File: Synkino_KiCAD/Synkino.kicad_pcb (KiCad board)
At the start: 2 copper layers, 93.3 x 82.3 mm, 181 parts, among them J1 Pwr, J10 EYE8_OUT, J11 EYE4_OUT, J12 2.5mm, J13 EYE5_OUT, J2 2.5mm, J3 3.5mm, J4 Micro_SD_Card_Det_Hirose_DM3AT, J5 EYE1_OUT, J6 EYE6_OUT, J7 EYE2_OUT, J8 EYE7_OUT, J9 EYE3_OUT, Q1 IRF7319, Q2 BC847, Q3 IRLML2244, SW1 SW_Push, SW2 Rotary_Encoder_Switch, SW3 SW_Push, U1 MCP1702T-5002E/MB, U10 ATMEGA328P-AU, U11 QRE1113, U12 QRE1113, U13 QRE1113, U14 QRE1113, U15 QRE1113, U16 QRE1113, U18 QRE1113, U2 ATMEGA328P-AU, U3 74HC4050, U4 SPIOLED128x64, U5 AP7312-1833W6-7, U6 74HC14, U7 VS1053B, U8 MAX4741, U9 QRE1113, X1 FTDIconn, X2 ICSP, X3 FTDIconn, X4 ICSP, Y1 16Mhz, Y2 12.288MHz, Y3 16Mhz

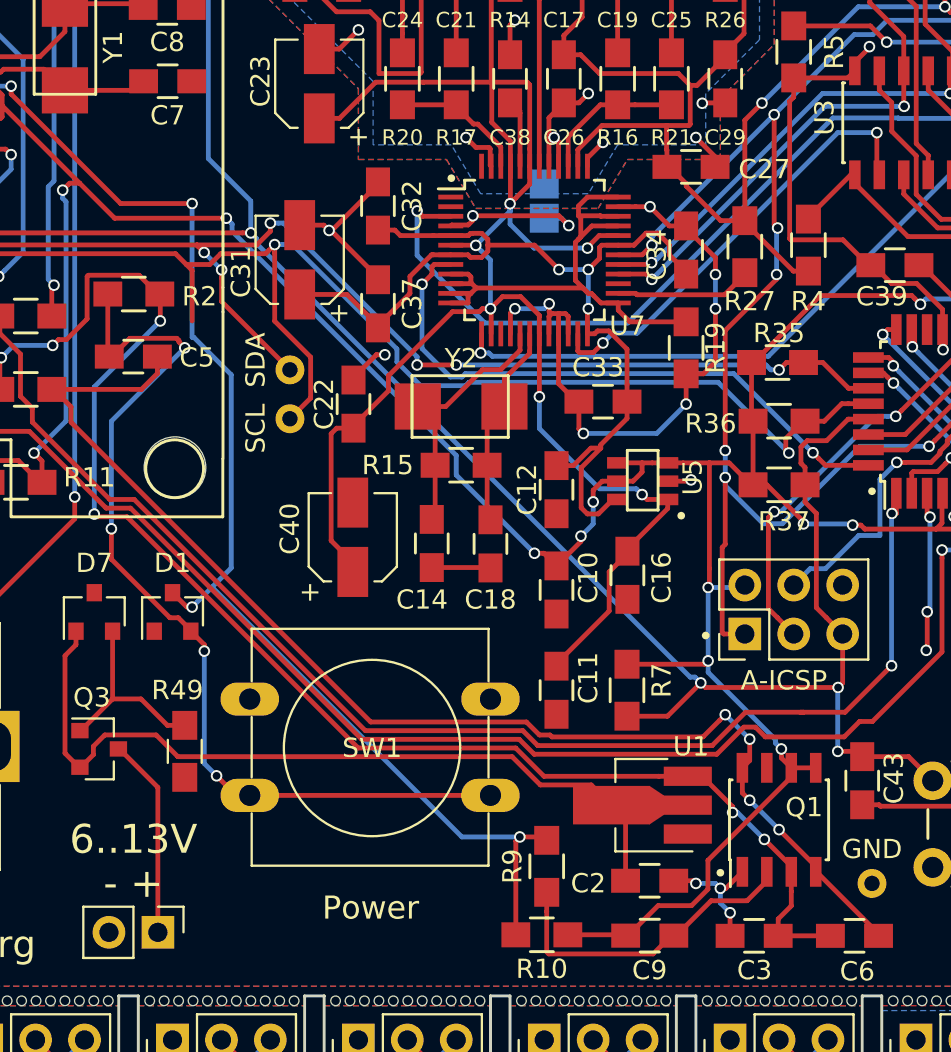
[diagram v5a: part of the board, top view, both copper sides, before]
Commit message: wider 1v8 lines
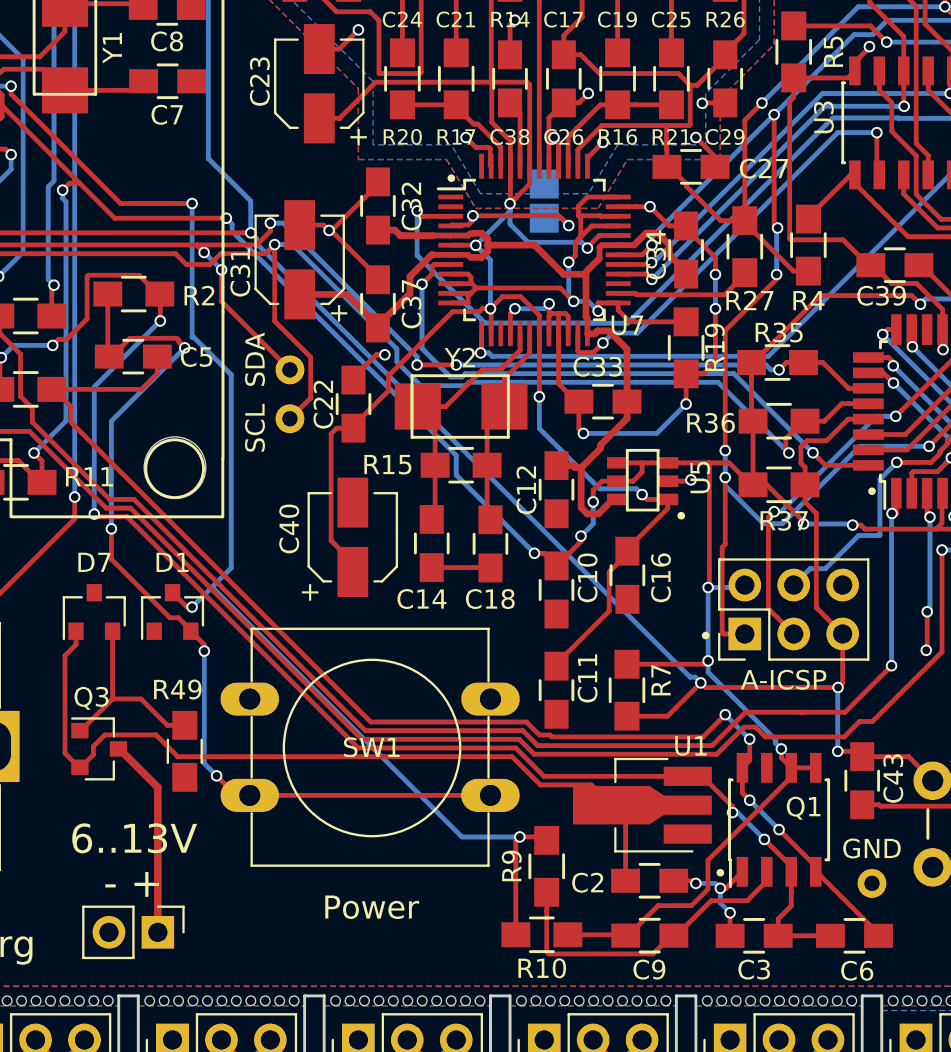
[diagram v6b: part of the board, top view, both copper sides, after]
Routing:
- net /SCL: track 74.7 -> 71.6 mm
- net +1V8: track 52.7 -> 51.6 mm, vias 3 -> 0
- net /GPIO_PLLDWN: track 29.8 -> 30.8 mm, vias 0 -> 3

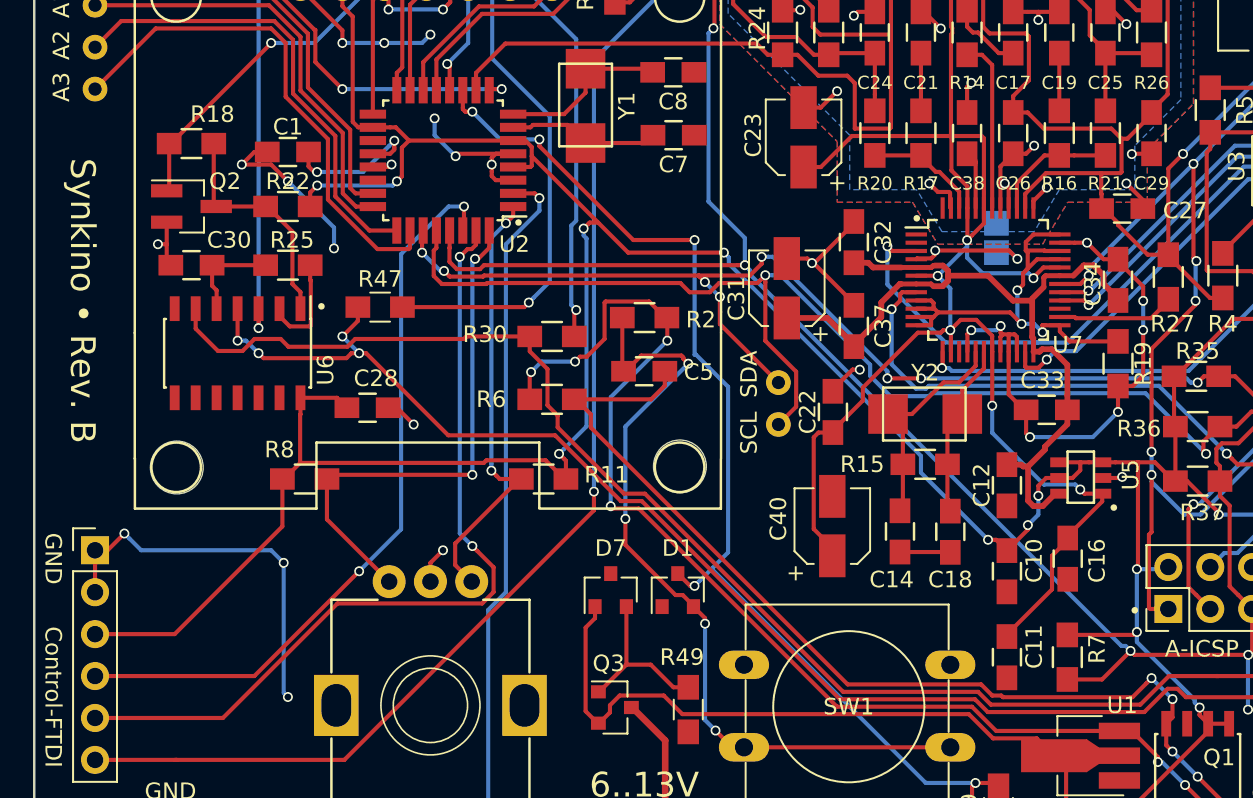
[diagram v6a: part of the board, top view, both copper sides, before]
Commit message: Fix Display Hole Position
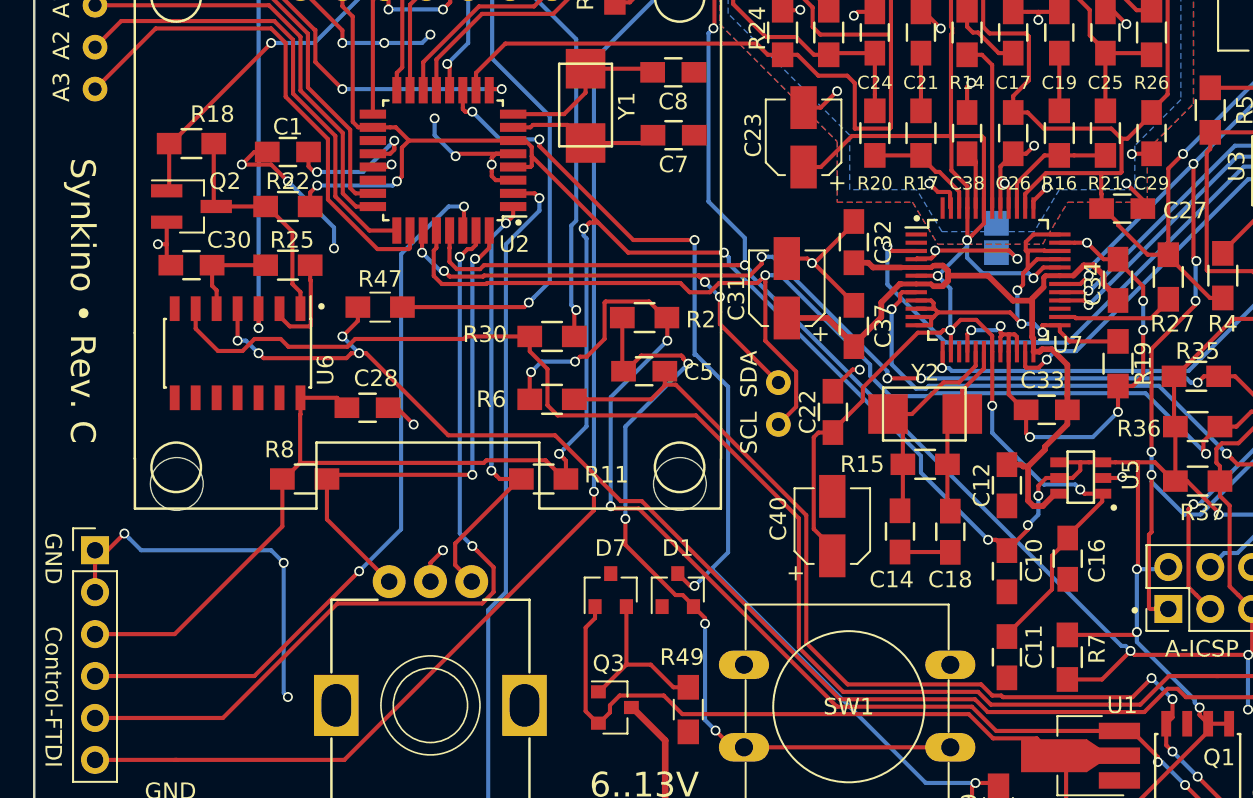
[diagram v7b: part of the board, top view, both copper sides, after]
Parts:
- moved   1.00 mm to (75.3, 81.1)
- moved   1.00 mm to (105.8, 81.0)
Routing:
- net /FlickImp: track 91.6 -> 95.8 mm
- net Net-(C5-Pad1): track 65.2 -> 64.2 mm
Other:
- board text added: "Synkino • Rev. C"
- board text removed: "Synkino • Rev. B"
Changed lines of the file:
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@@
     (links 375)
     (no_connects 0)
-    (area 66.599999 38.024999 160.095001 120.471001)
+    (area 57.856429 32.843999 168.838572 132.270286)
     (thickness 1.6)
     (drawings 107)
-    (tracks 2118)
+    (tracks 2119)
     (zones 0)
     (modules 181)
@@
     (mod_text_size 1 1)
     (mod_text_width 0.15)
-    (pad_size 3.048 1.7272)
-    (pad_drill 1.1)
+    (pad_size 3.2 3.2)
+    (pad_drill 3.2)
     (pad_to_mask_clearance 0.2)
     (aux_axis_origin 71.12 121.92)
@@
   )
   (module Mounting_Holes:MountingHole_3.2mm_M3_DIN965 (layer F.Cu)
-    (at 75.311 80.0735)
+    (at 75.311 81.0735)
     (descr "Mounting Hole 3.2mm, no annular, M3, DIN965")
     (tags "mounting hole 3.2mm no annular m3 din965")
@@
     (fp_circle (center 0 0) (end 2.8 0) (layer Cmts.User) (width 0.15))
     (fp_circle (center 0 0) (end 3.05 0) (layer F.CrtYd) (width 0.05))
-    (pad 1 np_thru_hole circle (at 0 0) (size 3.2 3.2) (drill 3.2) (layers *.Cu *.Mask))
+    (pad "" np_thru_hole circle (at 0 0) (size 3.2 3.2) (drill 3.2) (layers *.Cu *.Mask))
   )
   (module lib_fp:Eye_Mousebites (layer F.Cu)
@@
   )
   (module Mounting_Holes:MountingHole_3.2mm_M3_DIN965 (layer F.Cu)
-    (at 105.791 80.01)
+    (at 105.791 81.01)
     (descr "Mounting Hole 3.2mm, no annular, M3, DIN965")
     (tags "mounting hole 3.2mm no annular m3 din965")
@@
     (fp_circle (center 0 0) (end 2.8 0) (layer Cmts.User) (width 0.15))
     (fp_circle (center 0 0) (end 3.05 0) (layer F.CrtYd) (width 0.05))
-    (pad 1 np_thru_hole circle (at 0 0) (size 3.2 3.2) (drill 3.2) (layers *.Cu *.Mask))
+    (pad "" np_thru_hole circle (at 0 0.0635) (size 3.2 3.2) (drill 3.2) (layers *.Cu *.Mask))
   )
   (module Buttons_Switches_THT:SW_PUSH_6mm_h5mm (layer F.Cu)
@@
     (effects (font (size 1 1) (thickness 0.2)))
   )
-  (gr_text "Synkino • Rev. B" (at 69.596 69.85 270) (layer B.SilkS)
+  (gr_text "Synkino • Rev. C" (at 69.596 69.85 270) (layer B.SilkS)
     (effects (font (size 1.5 1.5) (thickness 0.3)) (justify mirror))
   )
@@
     (effects (font (size 1.4 1.4) (thickness 0.25)) (justify mirror))
   )
-  (gr_text "Synkino • Rev. B" (at 69.596 69.977 270) (layer F.SilkS)
+  (gr_text "Synkino • Rev. C" (at 69.596 69.977 270) (layer F.SilkS)
     (effects (font (size 1.5 1.5) (thickness 0.3)))
   )
@@
   (segment (start 85.461002 97.79) (end 100.584 82.667002) (width 0.25) (layer F.Cu) (net 5))
   (via (at 100.584 81.534) (size 0.6) (drill 0.4) (layers F.Cu B.Cu) (net 5))
-  (segment (start 133.210999 93.992001) (end 134.066001 93.136999) (width 0.25) (layer F.Cu) (net 6))
-  (segment (start 125.266643 93.892001) (end 125.366643 93.992001) (width 0.25) (layer F.Cu) (net 6))
-  (segment (start 125.366643 93.992001) (end 133.210999 93.992001) (width 0.25) (layer F.Cu) (net 6))
+  (segment (start 105.53841 75.057) (end 104.877 75.057) (width 0.25) (layer F.Cu) (net 6))
+  (segment (start 113.448988 82.967577) (end 105.53841 75.057) (width 0.25) (layer F.Cu) (net 6))
+  (segment (start 115.955597 93.216955) (end 113.448988 90.710346) (width 0.25) (layer F.Cu) (net 6))
+  (segment (start 124.042953 93.216955) (end 115.955597 93.216955) (width 0.25) (layer F.Cu) (net 6))
+  (segment (start 124.717999 93.892001) (end 124.042953 93.216955) (width 0.25) (layer F.Cu) (net 6))
+  (segment (start 125.266643 93.892001) (end 124.717999 93.892001) (width 0.25) (layer F.Cu) (net 6))
+  (segment (start 125.366643 93.992001) (end 125.266643 93.892001) (width 0.25) (layer F.Cu) (net 6))
+  (segment (start 133.210999 93.992001) (end 125.366643 93.992001) (width 0.25) (layer F.Cu) (net 6))
+  (segment (start 134.366 92.837) (end 133.210999 93.992001) (width 0.25) (layer F.Cu) (net 6))
+  (segment (start 113.448988 90.710346) (end 113.448988 82.967577) (width 0.25) (layer F.Cu) (net 6))
+  (segment (start 104.877 75.118) (end 104.877 75.057) (width 0.25) (layer F.Cu) (net 6))
+  (segment (start 104.877 75.057) (end 104.877 74.243) (width 0.25) (layer F.Cu) (net 6))
   (segment (start 99.394 75.946) (end 99.494 75.946) (width 0.25) (layer F.Cu) (net 6))
-  (segment (start 124.042953 93.216955) (end 124.717999 93.892001) (width 0.25) (layer F.Cu) (net 6))
-  (segment (start 134.066001 93.136999) (end 134.366 92.837) (width 0.25) (layer F.Cu) (net 6))
-  (segment (start 100.394 77.655356) (end 115.955597 93.216955) (width 0.25) (layer F.Cu) (net 6))
-  (segment (start 124.717999 93.892001) (end 125.266643 93.892001) (width 0.25) (layer F.Cu) (net 6))
-  (segment (start 100.394 76.846) (end 100.394 77.655356) (width 0.25) (layer F.Cu) (net 6))
-  (segment (start 99.494 75.946) (end 100.394 76.846) (width 0.25) (layer F.Cu) (net 6))
-  (segment (start 115.955597 93.216955) (end 124.042953 93.216955) (width 0.25) (layer F.Cu) (net 6))
   (segment (start 135.636 94.107) (end 135.636 95.217) (width 0.25) (layer F.Cu) (net 6))
   (segment (start 135.636 95.217) (end 135.255 95.598) (width 0.25) (layer F.Cu) (net 6))
@@
   (segment (start 99.394 75.946) (end 104.049 75.946) (width 0.25) (layer F.Cu) (net 6))
   (segment (start 104.049 75.946) (end 104.877 75.118) (width 0.25) (layer F.Cu) (net 6))
-  (segment (start 104.877 75.118) (end 104.877 74.243) (width 0.25) (layer F.Cu) (net 6))
   (segment (start 137.16 98.806) (end 139.065 100.711) (width 0.25) (layer F.Cu) (net 6))
   (segment (start 139.065 100.711) (end 139.065 100.998) (width 0.25) (layer F.Cu) (net 6))
@@
   (segment (start 134.332999 71.032001) (end 129.785001 71.032001) (width 0.25) (layer F.Cu) (net 56))
   (segment (start 129.71 70.957) (end 128.81 70.957) (width 0.25) (layer F.Cu) (net 56))
+  (segment (start 106.766001 76.921001) (end 112.998977 83.153977) (width 0.25) (layer F.Cu) (net 57))
+  (segment (start 112.998977 83.153977) (end 112.998977 90.989151) (width 0.25) (layer F.Cu) (net 57))
+  (segment (start 112.998977 90.989151) (end 115.676792 93.666966) (width 0.25) (layer F.Cu) (net 57))
+  (segment (start 98.383999 76.921001) (end 106.766001 76.921001) (width 0.25) (layer F.Cu) (net 57))
   (segment (start 96.694 73.036) (end 96.694 72.136) (width 0.25) (layer F.Cu) (net 57))
   (segment (start 97.769001 74.111001) (end 96.694 73.036) (width 0.25) (layer F.Cu) (net 57))
   (segment (start 97.769001 76.306003) (end 97.769001 74.111001) (width 0.25) (layer F.Cu) (net 57))
   (segment (start 98.383999 76.921001) (end 97.769001 76.306003) (width 0.25) (layer F.Cu) (net 57))
-  (segment (start 115.676792 93.666966) (end 103.669802 81.659976) (width 0.25) (layer F.Cu) (net 57))
   (segment (start 123.856553 93.666966) (end 115.676792 93.666966) (width 0.25) (layer F.Cu) (net 57))
   (segment (start 133.685992 94.442012) (end 124.631599 94.442012) (width 0.25) (layer F.Cu) (net 57))
@@
   (segment (start 138.43 92.71) (end 135.418004 92.71) (width 0.25) (layer F.Cu) (net 57))
   (segment (start 124.631599 94.442012) (end 123.856553 93.666966) (width 0.25) (layer F.Cu) (net 57))
-  (segment (start 103.669802 81.659976) (end 102.40208 81.659976) (width 0.25) (layer F.Cu) (net 57))
-  (segment (start 102.40208 81.659976) (end 98.383999 77.641895) (width 0.25) (layer F.Cu) (net 57))
-  (segment (start 98.383999 77.641895) (end 98.383999 76.921001) (width 0.25) (layer F.Cu) (net 57))
   (segment (start 138.265413 92.71) (end 138.43 92.71) (width 0.25) (layer F.Cu) (net 57))
   (segment (start 138.43 92.71) (end 140.589 92.71) (width 0.25) (layer F.Cu) (net 57))

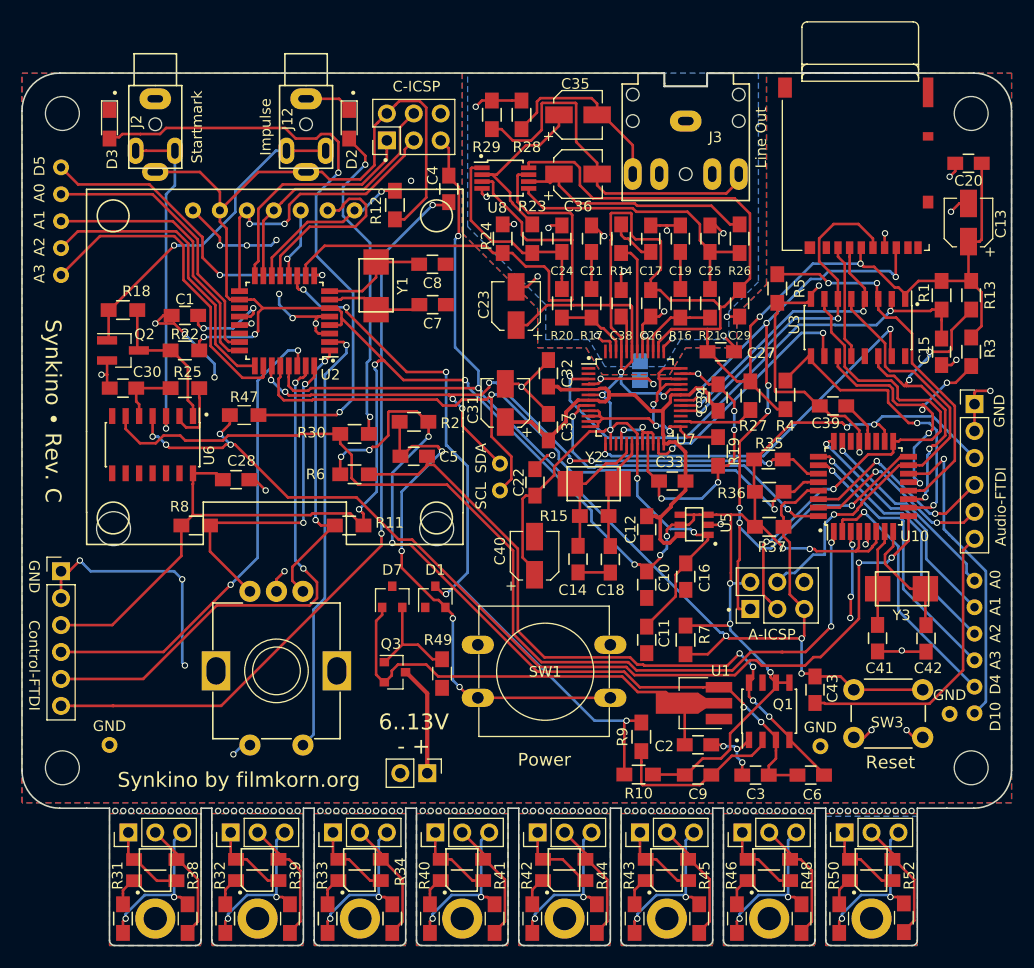
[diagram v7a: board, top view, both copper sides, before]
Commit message: Making FTDI and ICSP pins tighter
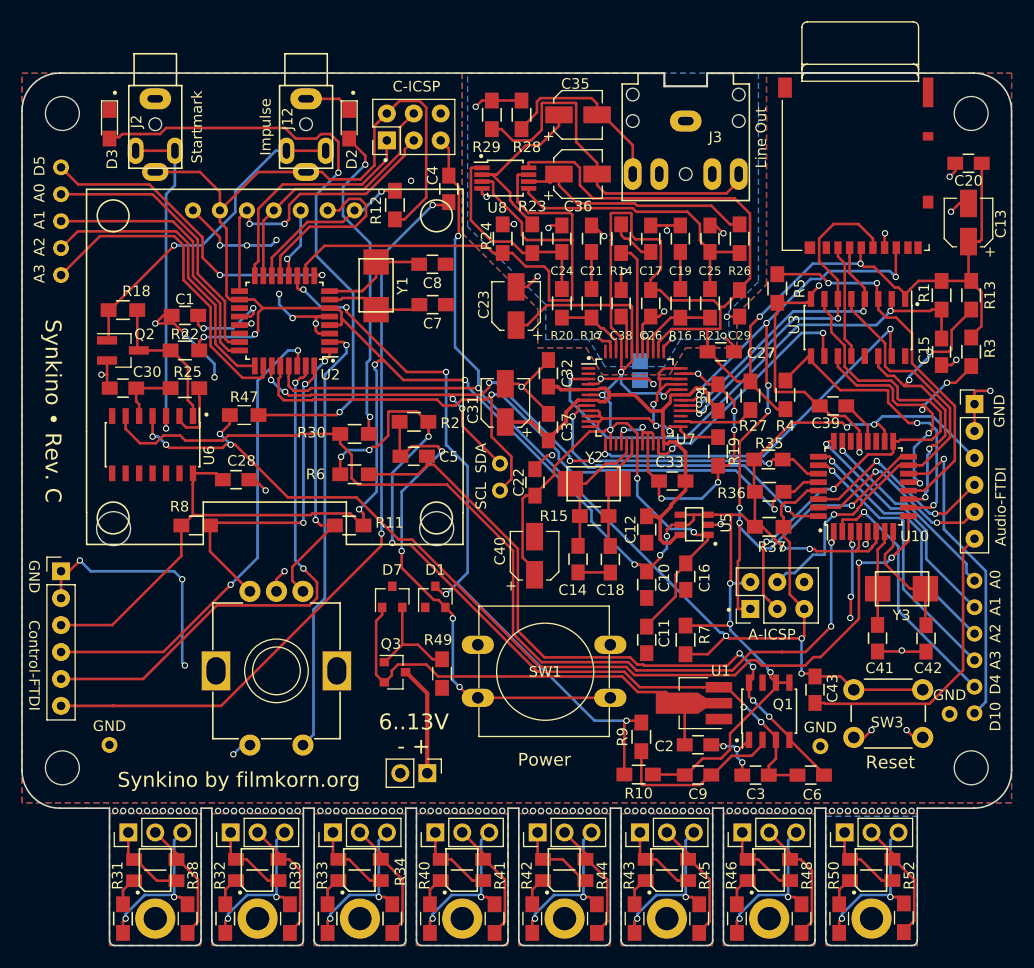
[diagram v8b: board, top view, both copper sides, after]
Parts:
- X1, X3: footprint Pin_Headers:Pin_Header_Straight_1x06_Pitch2.54mm -> lib_fp:Pin_Header_Straight_1x06_Pitch2.54mm
- X2, X4: footprint Pin_Headers:Pin_Header_Straight_2x03_Pitch2.54mm -> lib_fp:Pin_Header_Straight_2x03_Pitch2.54mm
